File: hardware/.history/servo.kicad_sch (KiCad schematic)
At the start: 37 parts, among them J1 servo, J2 Jack-DC, J3 swd, Q2 DMT64M8LSS, SW1 restart, SW2 buzzer, U1 AOZ1284PI, U3 STM32G030F6Px, U4 LDI1117-3.3U-DIO

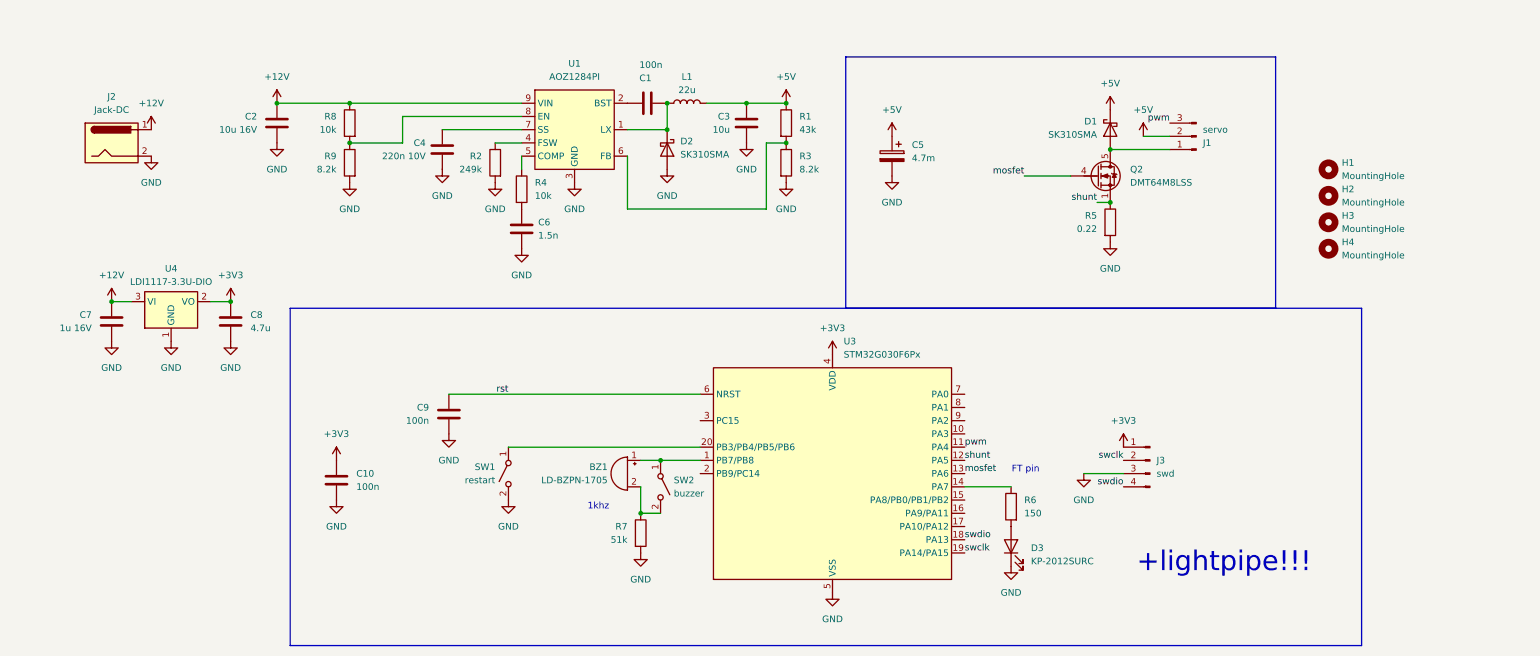
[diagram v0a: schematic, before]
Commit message: Fix false stall detection after restart
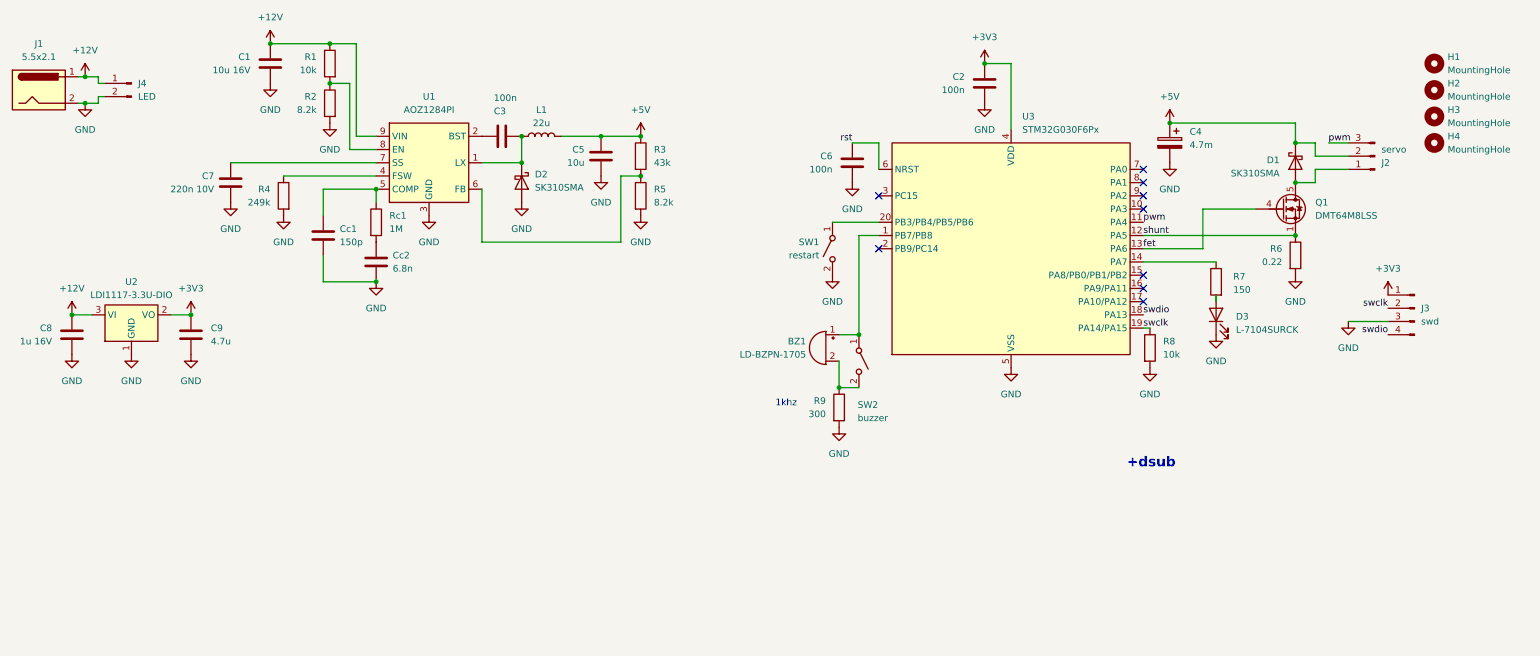
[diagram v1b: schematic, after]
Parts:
- added Cc1: 150p, Capacitor_SMD:C_0805_2012Metric_Pad1.18x1.45mm_HandSolder, symbol Device:C
- added J4: LED, Connector_Phoenix_MSTB:PhoenixContact_MSTBA_2,5_2-G-5,08_1x02_P5.08mm_Horizontal, symbol Connector:Conn_01x02_Pin
- added R8: 10k, Resistor_SMD:R_0805_2012Metric_Pad1.20x1.40mm_HandSolder, symbol Device:R
- Cc2: renamed from C6; value 1.5n -> 6.8n
- D3: value KP-2012SURC -> L-7104SURCK; footprint LED_SMD:LED_0805_2012Metric_Pad1.15x1.40mm_HandSolder -> LED_THT:LED_D3.0mm
- J1: renamed from J2; value Jack-DC -> 5.5x2.1; footprint Connector_BarrelJack:BarrelJack_CUI_PJ-102AH_Horizontal -> Connector_BarrelJack:BarrelJack_GCT_DCJ200-10-A_Horizontal
- R9: renamed from R7; value 51k -> 300
- Rc1: renamed from R4; value 10k -> 1M
- U1: footprint Package_SO:SOIC-8-1EP_3.9x4.9mm_P1.27mm_EP2.71x3.7mm -> Package_SO:SOIC-8-1EP_3.9x4.9mm_P1.27mm_EP2.29x3mm_diy
- renumbered C2 to C1, C10 to C2, C1 to C3, C5 to C4, C3 to C5, C9 to C6, C4 to C7, C7 to C8, C8 to C9, J1 to J2, Q2 to Q1, R8 to R1, R9 to R2, R1 to R3, R2 to R4, R3 to R5, R5 to R6, R6 to R7, U4 to U2
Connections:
- net +12V: now also J4.1 (Pin_1)
- net GND: now also Cc1.2, J4.2 (Pin_2), R8.2
- net swclk: now also R8.1
- net at Rc1.1, U1.5 (COMP): now also Cc1.1
- net mosfet renamed fet
- no-connect marks 0 -> 9
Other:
- note added: "+dsub"
- note removed: "+lightpipe!!!"
- note removed: "FT pin"
- moved on the sheet: BZ1, C1, C2, C3, C4, C5, C6, C7, C8, C9, Cc2, D1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

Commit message: Change buzzer supply to 12V, update PCB
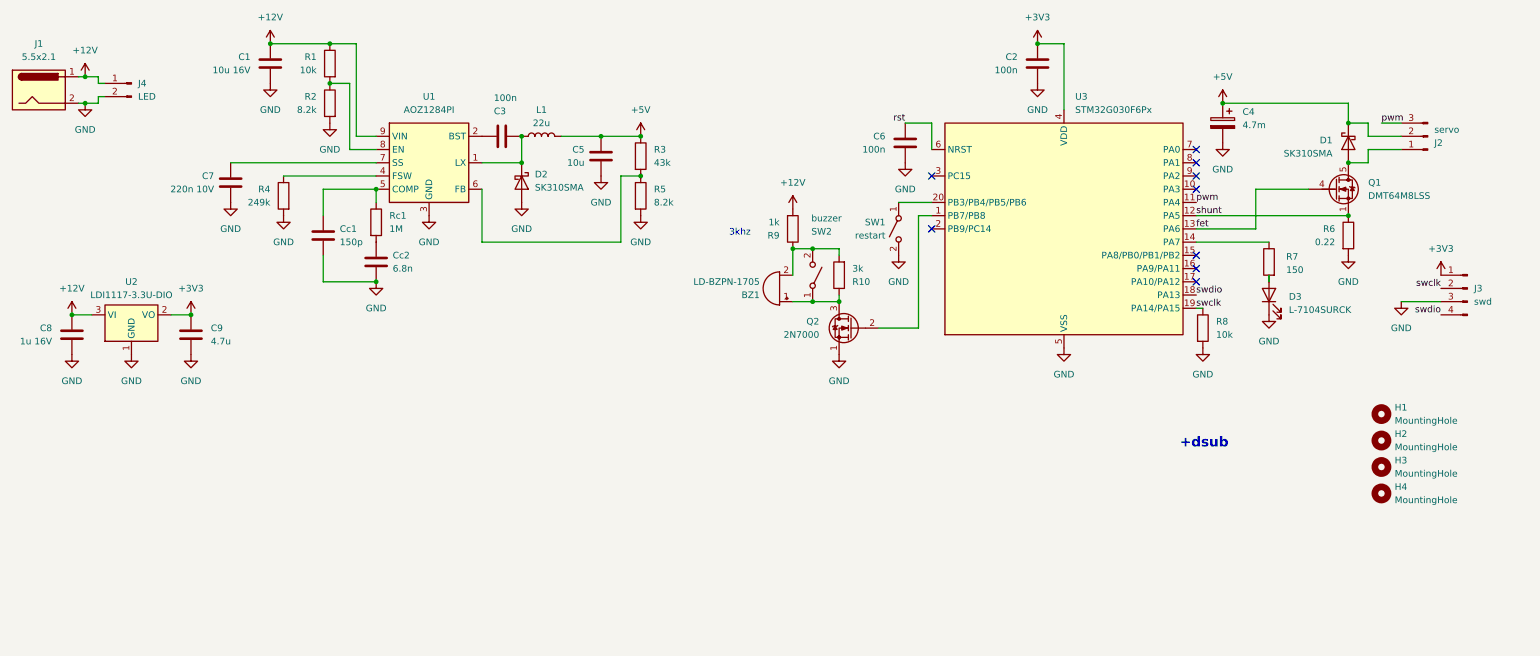
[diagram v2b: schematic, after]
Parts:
- added Q2: 2N7000, Package_TO_SOT_THT:TO-92_Inline, symbol Transistor_FET:2N7000
- added R10: 3k, Resistor_SMD:R_0805_2012Metric_Pad1.20x1.40mm_HandSolder, symbol Device:R
- J1: footprint Connector_BarrelJack:BarrelJack_GCT_DCJ200-10-A_Horizontal -> Connector_BarrelJack:BarrelJack_CUI_PJ-102AH_Horizontal
- J4: footprint Connector_Phoenix_MSTB:PhoenixContact_MSTBA_2,5_2-G-5,08_1x02_P5.08mm_Horizontal -> Connector_PinHeader_2.54mm:PinHeader_1x02_P2.54mm_Vertical
- R9: value 300 -> 1k
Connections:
- net +12V: now also R9.2
- net GND: now also Q2.1 (S); no longer R9.2
- net at BZ1.1 (+), SW2.1 (A): now also Q2.3 (D), R10.1; no longer U3.1 (PB7/PB8)
- net at BZ1.2 (-), R9.1, SW2.2 (B): now also R10.2
- new net: Q2.2 (G), U3.1 (PB7/PB8)
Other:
- note added: "3khz"
- note removed: "1khz"
- moved on the sheet: BZ1, C2, C4, C6, D1, D3, H1, H2, H3, H4, J2, J3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

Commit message: Start project conversion to DC motor
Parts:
- removed C4: 4.7m, Capacitor_THT:CP_Radial_D16.0mm_P7.50mm, symbol Device:C_Polarized
- added R11: 220, Resistor_SMD:R_0805_2012Metric_Pad1.20x1.40mm_HandSolder, symbol Device:R
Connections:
- net fet: now also R11.2; no longer Q1.4 (G)
- net pwm: no longer names the net of J2.3 (Pin_3)
- net pwm: no longer U3.11 (PA4)
- new net: Q1.4 (G), R11.1
- no-connect marks 9 -> 11
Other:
- note added: "5v i 6v pakeist kompensacija pridetas r11, isimtas 4.7mf perdaryt korpusa?"
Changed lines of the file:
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@@
 	(generator_version "10.0")
 	(paper "A4")
+	(text "5v i 6v\npakeist kompensacija\npridetas r11, isimtas 4.7mf\nperdaryt korpusa?"
+		(exclude_from_sim no)
+		(at 183.388 85.852 0)
+		(effects
+			(font
+				(size 1.27 1.27)
+			)
+			(justify left)
+		)
+	)
 	(text "3khz"
 		(exclude_from_sim no)
@@
 	)
 	(junction
-		(at 238.76 22.86)
-		(diameter 0)
-		(color 0 0 0 0)
-	)
-	(junction
 		(at 119.38 29.21)
 		(diameter 0)
@@
 	)
 	(no_connect
+		(at 233.68 41.91)
+	)
+	(no_connect
 		(at 182.88 46.99)
 	)
@@
 	)
 	(no_connect
+		(at 273.05 26.67)
+	)
+	(no_connect
 		(at 233.68 39.37)
 	)
@@
 	(wire
 		(pts
-			(xy 67.31 19.05) (xy 71.12 19.05)
+			(xy 254 39.37) (xy 255.27 39.37)
 		)
 		(stroke
@@
 	(wire
 		(pts
-			(xy 266.7 29.21) (xy 273.05 29.21)
+			(xy 67.31 19.05) (xy 71.12 19.05)
 		)
 		(stroke
@@
 	(wire
 		(pts
-			(xy 111.76 29.21) (xy 119.38 29.21)
+			(xy 266.7 29.21) (xy 273.05 29.21)
 		)
 		(stroke
@@
 	(wire
 		(pts
-			(xy 273.05 26.67) (xy 269.24 26.67)
+			(xy 111.76 29.21) (xy 119.38 29.21)
 		)
 		(stroke
@@
 	(wire
 		(pts
-			(xy 245.11 39.37) (xy 255.27 39.37)
-		)
-		(stroke
-			(width 0)
-			(type default)
-		)
-	)
-	(wire
-		(pts
 			(xy 72.39 11.43) (xy 72.39 29.21)
 		)
@@
 	(wire
 		(pts
-			(xy 176.53 41.91) (xy 182.88 41.91)
+			(xy 245.11 39.37) (xy 246.38 39.37)
 		)
 		(stroke
@@
 	(wire
 		(pts
-			(xy 266.7 29.21) (xy 266.7 26.67)
+			(xy 176.53 41.91) (xy 182.88 41.91)
 		)
 		(stroke
@@
 	(wire
 		(pts
-			(xy 262.89 22.86) (xy 262.89 26.67)
+			(xy 266.7 29.21) (xy 266.7 26.67)
 		)
 		(stroke
@@
 	(wire
 		(pts
-			(xy 238.76 22.86) (xy 262.89 22.86)
-		)
-		(stroke
-			(width 0)
-			(type default)
-		)
-	)
-	(wire
-		(pts
 			(xy 66.04 52.07) (xy 66.04 57.15)
 		)
@@
 		)
 	)
-	(label "pwm"
-		(at 233.68 41.91 0)
-		(effects
-			(font
-				(size 1.27 1.27)
-			)
-			(justify left bottom)
-		)
-	)
-	(label "pwm"
-		(at 269.24 26.67 0)
-		(effects
-			(font
-				(size 1.27 1.27)
-			)
-			(justify left bottom)
-		)
-	)
 	(label "swclk"
 		(at 233.68 62.23 0)
@@
 	)
 	(symbol
-		(lib_id "Device:C_Polarized")
-		(at 238.76 26.67 0)
-		(mirror y)
-		(unit 1)
-		(body_style 1)
-		(exclude_from_sim no)
-		(in_bom yes)
-		(on_board yes)
-		(in_pos_files yes)
-		(dnp no)
-		(fields_autoplaced yes)
-		(property "Reference" "C4"
-			(at 242.57 24.5109 0)
-			(show_name no)
-			(do_not_autoplace no)
-			(effects
-				(font
-					(size 1.27 1.27)
-				)
-				(justify right)
-			)
-		)
-		(property "Value" "4.7m"
-			(at 242.57 27.0509 0)
-			(show_name no)
-			(do_not_autoplace no)
-			(effects
-				(font
-					(size 1.27 1.27)
-				)
-				(justify right)
-			)
-		)
-		(property "Footprint" "Capacitor_THT:CP_Radial_D16.0mm_P7.50mm"
-			(at 237.7948 30.48 0)
-			(hide yes)
-			(show_name no)
-			(do_not_autoplace no)
-			(effects
-				(font
-					(size 1.27 1.27)
-				)
-			)
-		)
-		(property "Datasheet" ""
-			(at 238.76 26.67 0)
-			(hide yes)
-			(show_name no)
-			(do_not_autoplace no)
-			(effects
-				(font
-					(size 1.27 1.27)
-				)
-			)
-		)
-		(property "Description" "Polarized capacitor"
-			(at 238.76 26.67 0)
-			(hide yes)
-			(show_name no)
-			(do_not_autoplace no)
-			(effects
-				(font
-					(size 1.27 1.27)
-				)
-			)
-		)
-		(pin "1"
-		)
-		(pin "2"
-		)
-		(instances
-			(project "servo"
-				(path "/868aa114-83f2-46f3-8e6d-8a7027303d9c"
-					(reference "C4")
-					(unit 1)
-				)
-			)
-		)
-	)
-	(symbol
 		(lib_id "Device:C")
 		(at 48.26 38.1 0)
@@
 	(symbol
 		(lib_id "power:GND")
-		(at 238.76 30.48 0)
-		(mirror y)
+		(at 67.31 26.67 0)
 		(unit 1)
 		(body_style 1)
@@
 		(dnp no)
 		(fields_autoplaced yes)
-		(property "Reference" "#PWR010"
-			(at 238.76 36.83 0)
+		(property "Reference" "#PWR07"
+			(at 67.31 33.02 0)
 			(hide yes)
 			(show_name no)
@@
 		)
 		(property "Value" "GND"
-			(at 238.76 35.56 0)
+			(at 67.31 31.75 0)
 			(show_name no)
 			(do_not_autoplace no)
@@
 		)
 		(property "Footprint" ""
-			(at 238.76 30.48 0)
+			(at 67.31 26.67 0)
 			(hide yes)
 			(show_name no)
@@
 		)
 		(property "Datasheet" ""
-			(at 238.76 30.48 0)
+			(at 67.31 26.67 0)
 			(hide yes)
 			(show_name no)
@@
 		)
 		(property "Description" "Power symbol creates a global label with name \"GND\" , ground"
-			(at 238.76 30.48 0)
+			(at 67.31 26.67 0)
 			(hide yes)
 			(show_name no)
@@
 			(project "servo"
 				(path "/868aa114-83f2-46f3-8e6d-8a7027303d9c"
-					(reference "#PWR010")
+					(reference "#PWR07")
 					(unit 1)
 				)
@@
 	)
 	(symbol
-		(lib_id "power:GND")
-		(at 67.31 26.67 0)
+		(lib_id "Device:L")
+		(at 107.95 29.21 90)
 		(unit 1)
 		(body_style 1)
@@
 		(dnp no)
 		(fields_autoplaced yes)
-		(property "Reference" "#PWR07"
-			(at 67.31 33.02 0)
-			(hide yes)
+		(property "Reference" "L1"
+			(at 107.95 24.13 90)
 			(show_name no)
 			(do_not_autoplace no)
@@
 			)
 		)
-		(property "Value" "GND"
-			(at 67.31 31.75 0)
+		(property "Value" "22u"
+			(at 107.95 26.67 90)
 			(show_name no)
 			(do_not_autoplace no)
@@
 			)
 		)
-		(property "Footprint" ""
-			(at 67.31 26.67 0)
+		(property "Footprint" "Inductor_SMD:LD2-HV"
+			(at 107.95 29.21 0)
 			(hide yes)
 			(show_name no)
@@
 		)
 		(property "Datasheet" ""
-			(at 67.31 26.67 0)
+			(at 107.95 29.21 0)
 			(hide yes)
 			(show_name no)
@@
 			)
 		)
-		(property "Description" "Power symbol creates a global label with name \"GND\" , ground"
-			(at 67.31 26.67 0)
+		(property "Description" "Inductor"
+			(at 107.95 29.21 0)
 			(hide yes)
 			(show_name no)
@@
 		(pin "1"
 		)
+		(pin "2"
+		)
 		(instances
 			(project "servo"
 				(path "/868aa114-83f2-46f3-8e6d-8a7027303d9c"
-					(reference "#PWR07")
+					(reference "L1")
 					(unit 1)
 				)
@@
 	)
 	(symbol
-		(lib_id "Device:L")
-		(at 107.95 29.21 90)
+		(lib_id "Device:R")
+		(at 250.19 39.37 270)
 		(unit 1)
 		(body_style 1)
@@
 		(in_pos_files yes)
 		(dnp no)
-		(fields_autoplaced yes)
-		(property "Reference" "L1"
-			(at 107.95 24.13 90)
+		(property "Reference" "R11"
+			(at 252.222 34.544 90)
 			(show_name no)
 			(do_not_autoplace no)
@@
 					(size 1.27 1.27)
 				)
+				(justify right)
 			)
 		)
-		(property "Value" "22u"
-			(at 107.95 26.67 90)
+		(property "Value" "220"
+			(at 252.222 37.084 90)
 			(show_name no)
 			(do_not_autoplace no)
@@
 					(size 1.27 1.27)
 				)
+				(justify right)
 			)
 		)
-		(property "Footprint" "Inductor_SMD:LD2-HV"
-			(at 107.95 29.21 0)
+		(property "Footprint" "Resistor_SMD:R_0805_2012Metric_Pad1.20x1.40mm_HandSolder"
+			(at 250.19 37.592 90)
 			(hide yes)
 			(show_name no)
@@
 		)
 		(property "Datasheet" ""
-			(at 107.95 29.21 0)
+			(at 250.19 39.37 0)
 			(hide yes)
 			(show_name no)
@@
 			)
 		)
-		(property "Description" "Inductor"
-			(at 107.95 29.21 0)
+		(property "Description" "Resistor"
+			(at 250.19 39.37 0)
 			(hide yes)
 			(show_name no)
@@
 			(project "servo"
 				(path "/868aa114-83f2-46f3-8e6d-8a7027303d9c"
-					(reference "L1")
+					(reference "R11")
 					(unit 1)
 				)
@@
 		(dnp no)
 		(property "Reference" "D1"
-			(at 259.842 29.972 90)
+			(at 259.842 26.162 90)
 			(show_name no)
 			(do_not_autoplace no)
@@
 		)
 		(property "Value" "SK310SMA"
-			(at 259.842 32.512 90)
+			(at 259.842 28.702 90)
 			(show_name no)
 			(do_not_autoplace no)
@@
 	(symbol
 		(lib_id "power:+5V")
-		(at 238.76 22.86 0)
+		(at 262.89 26.67 0)
 		(mirror y)
 		(unit 1)
@@
 		(fields_autoplaced yes)
 		(property "Reference" "#PWR08"
-			(at 238.76 26.67 0)
+			(at 262.89 30.48 0)
 			(hide yes)
 			(show_name no)
@@
 		)
 		(property "Value" "+5V"
-			(at 238.76 17.78 0)
+			(at 262.89 21.59 0)
 			(show_name no)
 			(do_not_autoplace no)
@@
 		)
 		(property "Footprint" ""
-			(at 238.76 22.86 0)
+			(at 262.89 26.67 0)
 			(hide yes)
 			(show_name no)
@@
 		)
 		(property "Datasheet" ""
-			(at 238.76 22.86 0)
+			(at 262.89 26.67 0)
 			(hide yes)
 			(show_name no)
@@
 		)
 		(property "Description" "Power symbol creates a global label with name \"+5V\""
-			(at 238.76 22.86 0)
+			(at 262.89 26.67 0)
 			(hide yes)
 			(show_name no)
